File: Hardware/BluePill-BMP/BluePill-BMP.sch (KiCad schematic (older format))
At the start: 18 parts, among them J1 SWO, J2 JTAG, J3 GDB_COMM, J4 VCC, J5 GND, J6 LogicAna, U1 FT232RL_Breakout, U2 STM32F103 BluePill

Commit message: - JTAG over SPI
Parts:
- removed J1: SWO, Connector_PinHeader_2.54mm:PinHeader_1x02_P2.54mm_Vertical, symbol Connector_Generic:Conn_01x02
- added J1: Conn_01x08, Connector_PinHeader_2.54mm:PinHeader_1x08_P2.54mm_Vertical, symbol Connector_Generic:Conn_01x08
- added J7: Conn_01x11, Connector_PinHeader_2.54mm:PinHeader_1x11_P2.54mm_Vertical, symbol Connector_Generic:Conn_01x11
- added J8, J9: Conn_01x05, Connector_PinHeader_2.54mm:PinHeader_1x05_P2.54mm_Vertical, symbol Connector_Generic:Conn_01x05
- J3: footprint Connector_PinHeader_2.54mm:PinHeader_1x04_P2.54mm_Horizontal -> Connector_Molex:Molex_KK-254_AE-6410-04A_1x04_P2.54mm_Vertical
- J4: footprint Connector_PinHeader_2.54mm:PinHeader_1x03_P2.54mm_Vertical -> Connector_PinHeader_2.54mm:PinHeader_1x02_P2.54mm_Vertical; symbol Connector_Generic:Conn_01x03 -> Connector_Generic:Conn_01x02
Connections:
- net +3V3: no longer J4.3 (Pin_3)
- net BRST: now also U2.27 (PA2), J7.11 (Pin_11); no longer U2.5 (PA8)
- net BTCK: now also U2.26 (PA1), J7.8 (Pin_8)
- net BTDI: now also J7.6 (Pin_6)
- net BTDO: now also J7.7 (Pin_7)
- net BTEST: now also U2.29 (PA4), J7.9 (Pin_9); no longer U2.26 (PA1)
- net BTMS: now also U2.28 (PA3), J7.10 (Pin_10); no longer U2.29 (PA4)
- net GDB_RX: now also U2.7 (PA10); no longer U2.28 (PA3)
- net GDB_TX: now also U2.6 (PA9); no longer U2.27 (PA2)
- net LEDG: now also J7.5 (Pin_5)
- net TRACESWO: now also J1.2 (Pin_2)
- net VREF: now also J9.1 (Pin_1)
- net PB12: now reaches U2.1 (PB12)
- net PB12: now also J8.1 (Pin_1)
- net PA15: now reaches U2.10 (PA15)
- net PA15: now also J1.1 (Pin_1)
- net PB4: now reaches U2.12 (PB4)
- net PB4: now also J1.3 (Pin_3)
- net PB5: now reaches U2.13 (PB5)
- net PB5: now also J1.4 (Pin_4)
- net PB6: now reaches U2.14 (PB6)
- net PB6: now also J1.5 (Pin_5)
- net PB7: now reaches U2.15 (PB7)
- net PB7: now also J1.6 (Pin_6)
- net PB8: now reaches U2.16 (PB8)
- net PB8: now also J1.7 (Pin_7)
- net PB9: now reaches U2.17 (PB9)
- net PB9: now also J1.8 (Pin_8)
- net PB13: now reaches U2.2 (PB13)
- net PB13: now also J8.2 (Pin_2)
- net VBAT: now reaches U2.21 (VBat)
- net VBAT: now also J9.5 (Pin_5)
- net PC13: now reaches U2.22 (PC13)
- net PC13: now also J9.4 (Pin_4)
- net PC14: now reaches U2.23 (PC14)
- net PC14: now also J9.3 (Pin_3)
- net PC15: now reaches U2.24 (PC15)
- net PC15: now also J9.2 (Pin_2)
- net PB14: now reaches U2.3 (PB14)
- net PB14: now also J8.3 (Pin_3)
- net PB1: now reaches U2.34 (PB1)
- net PB1: now also J7.4 (Pin_4)
- net PB10: now reaches U2.35 (PB10)
- net PB10: now also J7.3 (Pin_3)
- net PB11: now reaches U2.36 (PB11)
- net PB11: now also J7.2 (Pin_2)
- net RST: now reaches U2.37 (RST)
- net RST: now also J7.1 (Pin_1)
- net PB15: now reaches U2.4 (PB15)
- net PB15: now also J8.4 (Pin_4)
- new net PA8: J8.5 (Pin_5), U2.5 (PA8)
- no-connect marks 47 -> 26
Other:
- note added: "USART1: GDB Port\nTRACESWO: External device or Optional FT232 Breakout\nSPI: JTAG interface (also supports bit-bang)\nTIM2: JTMS signal generation\nGPI: LEDG, JTAG (partial)"
- moved on the sheet: D1, J3, J5, R7, R8, R9, U1

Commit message: Updated Hardware Schematics and Boards
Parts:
- removed J9: Conn_01x05, Connector_PinHeader_2.54mm:PinHeader_1x05_P2.54mm_Vertical, symbol Connector_Generic:Conn_01x05
- removed R1: 330, Resistor_THT:R_Axial_DIN0204_L3.6mm_D1.6mm_P7.62mm_Horizontal, symbol Device:R
- added C1: 100nF, Capacitor_THT:C_Disc_D4.3mm_W1.9mm_P5.00mm, symbol Device:C
- added R10, R11, R9: 330, Resistor_THT:R_Axial_DIN0204_L3.6mm_D1.6mm_P7.62mm_Horizontal, symbol Device:R
- J1: value Conn_01x08 -> Conn_01x07; footprint Connector_PinHeader_2.54mm:PinHeader_1x08_P2.54mm_Vertical -> Connector_PinHeader_2.54mm:PinHeader_1x07_P2.54mm_Vertical; symbol Connector_Generic:Conn_01x08 -> Connector_Generic:Conn_01x07
- J3: renamed from J7; footprint Connector_PinHeader_2.54mm:PinHeader_1x11_P2.54mm_Vertical -> Connector_PinHeader_2.54mm:PinHeader_1x13_P2.54mm_Vertical; symbol Connector_Generic:Conn_01x11 -> Connector_Generic:Conn_01x13
- J8: renamed from J6; footprint Connector_PinHeader_2.54mm:PinHeader_1x06_P2.54mm_Vertical -> Connector_PinHeader_2.54mm:PinHeader_1x07_P2.54mm_Vertical; symbol Connector_Generic:Conn_01x06 -> Connector_Generic:Conn_01x07
- renumbered J8 to J2, J3 to J4, J4 to J5, J5 to J6, J2 to J7, R7 to R1, R8 to R2, R9 to R3, R2 to R4, R3 to R5, R4 to R6, R5 to R7, R6 to R8
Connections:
- net PA8 is gone; now on net BTEST: J2.5 (Pin_5), U2.5 (PA8)
- net PB12 is gone; now on net BRST: J2.1 (Pin_1), U2.1 (PB12)
- net PB13 is gone; now on net BTCK: J2.2 (Pin_2), U2.2 (PB13)
- net PB14 is gone; now on net JTDO: J2.3 (Pin_3), U2.3 (PB14)
- net PB15 is gone; now on net BTDI: J2.4 (Pin_4), U2.4 (PB15)
- net +3V3: now also C1.1
- net BRST: no longer J3.11 (Pin_11), U2.27 (PA2)
- net BTCK: now also J1.4 (Pin_4), U2.14 (PB6); no longer J3.8 (Pin_8), U2.26 (PA1), U2.30 (PA5)
- net BTDI: now also R11.2; no longer J3.6 (Pin_6), U2.32 (PA7)
- net BTEST: no longer J3.9 (Pin_9), U2.29 (PA4)
- net BTMS: now also J1.5 (Pin_5), U2.15 (PB7); no longer J3.10 (Pin_10), U2.28 (PA3)
- net GND: now also J7.13 (Pin_13), J8.7 (Pin_7), C1.2
- net JTDO: now also R11.1
- net LEDG: now also J3.10 (Pin_10); no longer J3.5 (Pin_5)
- net PB1: now also J3.11 (Pin_11); no longer J3.4 (Pin_4)
- net PB5: now also J1.3 (Pin_3); no longer J1.4 (Pin_4)
- net PB8: now also J1.6 (Pin_6); no longer J1.7 (Pin_7)
- net PB9: now also J1.7 (Pin_7); no longer J1.8 (Pin_8)
- net PC13: now also J3.1 (Pin_1)
- net TRACESWO: now also J1.1 (Pin_1); no longer J1.2 (Pin_2)
- net VREF: now also J3.2 (Pin_2)
- net JTXD: now reaches J7.12 (Pin_12)
- net JTXD: now also R9.2
- net JRXD: now reaches J7.14 (Pin_14)
- net JRXD: now also R10.2
- net BTDO renamed PA5
- net PA5: now also U2.30 (PA5); no longer U2.31 (PA6)
- net PA15: no longer names the net of U2.10 (PA15)
- net PA15: no longer J1.1 (Pin_1)
- net PB10 renamed BTXD
- net BTXD: now also J3.12 (Pin_12), R10.1; no longer J3.3 (Pin_3)
- net PB11 renamed BRXD
- net BRXD: now also J3.13 (Pin_13), R9.1; no longer J3.2 (Pin_2)
- net PB4: no longer names the net of U2.12 (PB4)
- net PB4: no longer J1.3 (Pin_3)
- removed net PB6: J1.5 (Pin_5), U2.14 (PB6)
- removed net PB7: J1.6 (Pin_6), U2.15 (PB7)
- net PC14: no longer names the net of U2.23 (PC14)
- net PC15: no longer names the net of U2.24 (PC15)
- net RST: no longer names the net of U2.37 (RST)
- net RST: no longer J3.1 (Pin_1)
- net VBAT: no longer names the net of U2.21 (VBat)
- new net PA1: J3.3 (Pin_3), U2.26 (PA1)
- new net PA2: J3.4 (Pin_4), U2.27 (PA2)
- new net PA3: J3.5 (Pin_5), U2.28 (PA3)
- new net PA4: J3.6 (Pin_6), U2.29 (PA4)
- new net PA6: J3.8 (Pin_8), U2.31 (PA6)
- new net PA7: J3.9 (Pin_9), U2.32 (PA7)
- no-connect marks 26 -> 30
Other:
- note added: "SN74CB3T1G125\nSWO switch"
- moved on the sheet: J2

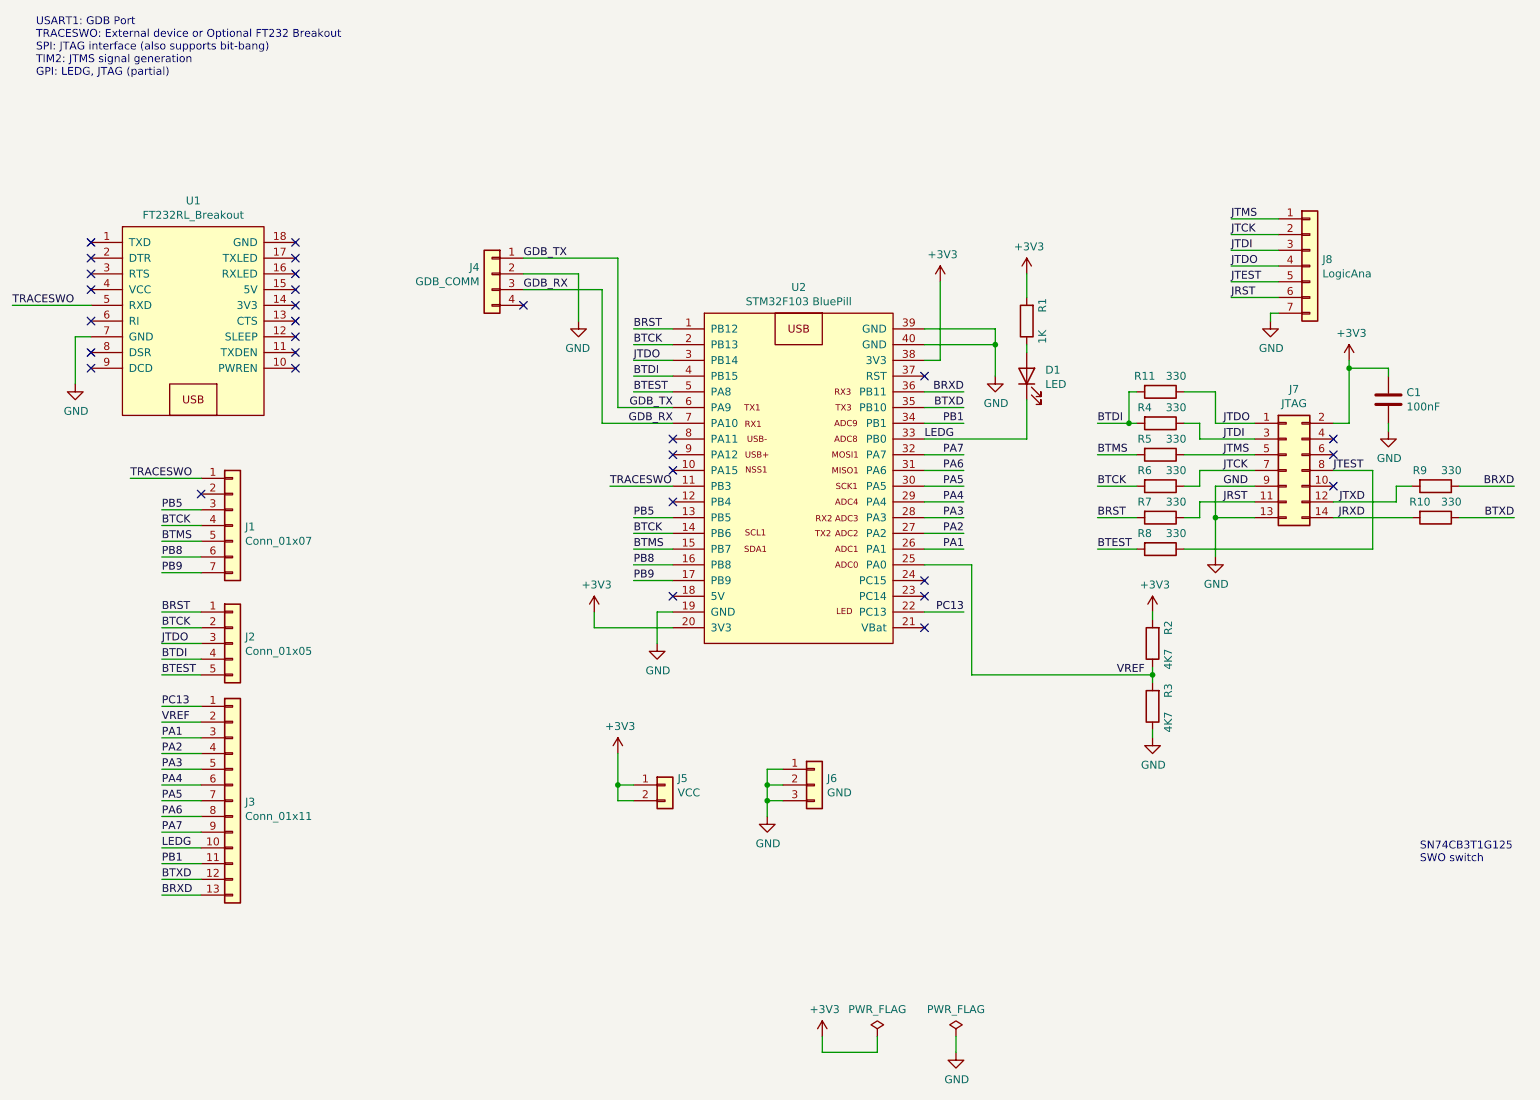
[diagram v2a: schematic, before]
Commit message: Fixed Bluepill schematics
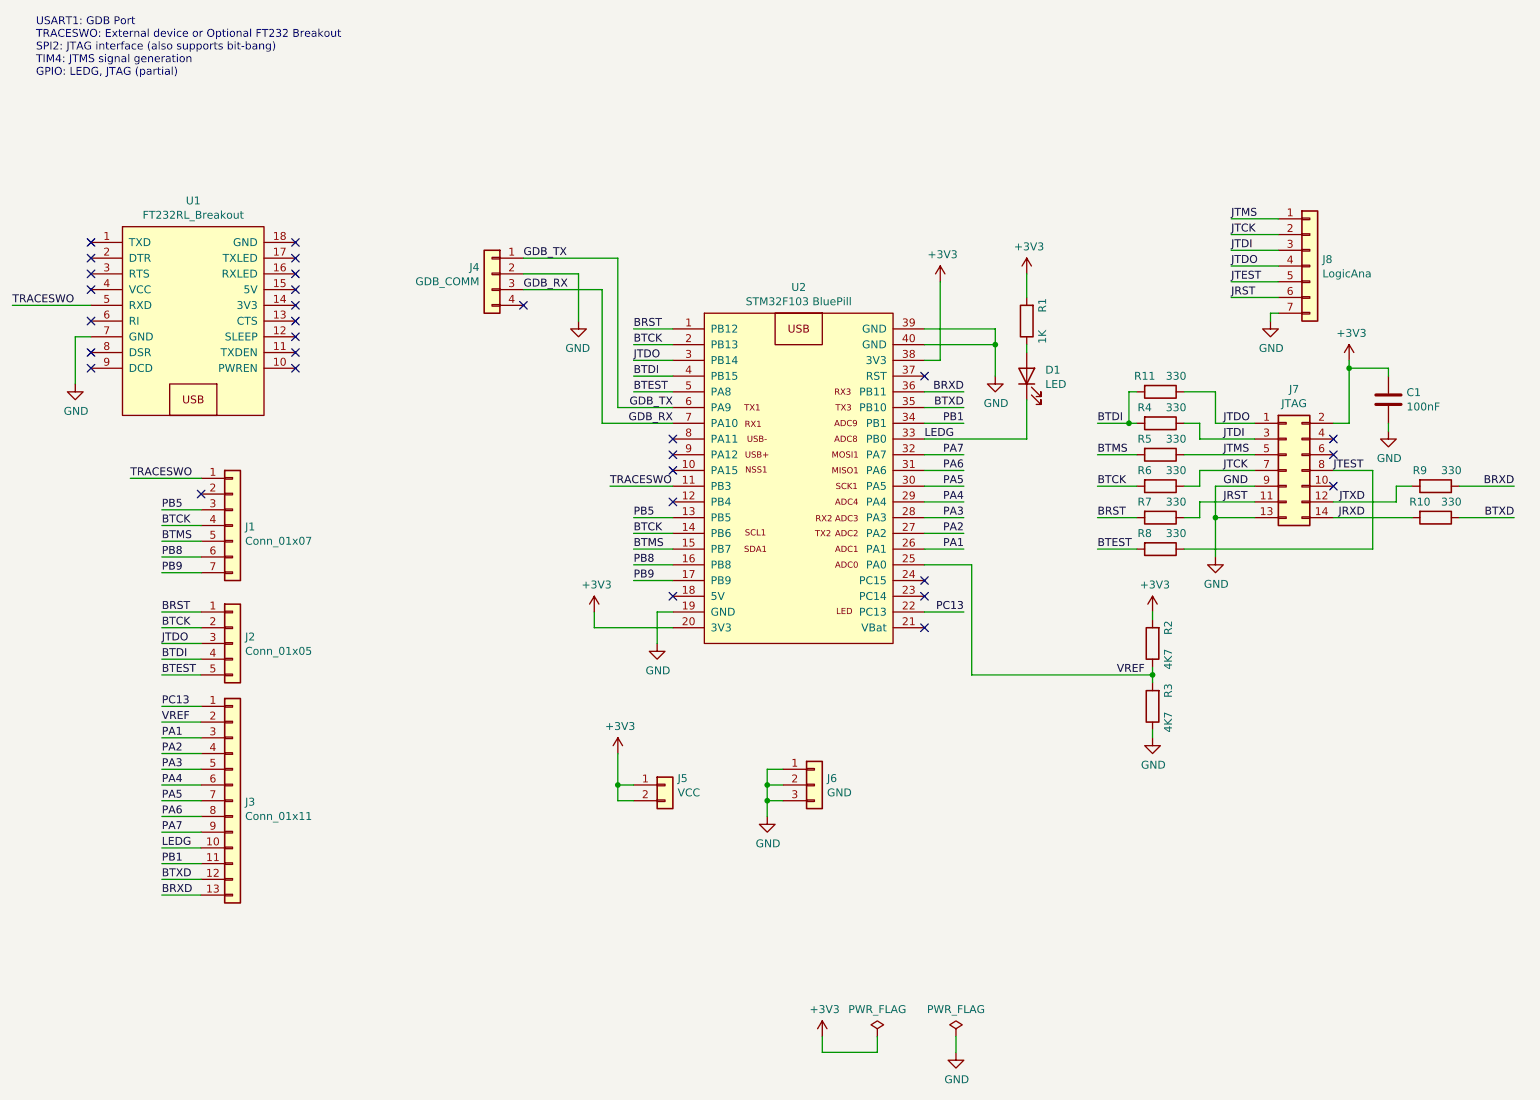
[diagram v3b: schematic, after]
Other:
- note added: "USART1: GDB Port\nTRACESWO: External device or Optional FT232 Breakout\nSPI2: JTAG interface (also supports bit-bang)\nTIM4: JTMS signal generation\nGPIO: LEDG, JTAG (partial)"
- note removed: "SN74CB3T1G125\nSWO switch"
- note removed: "USART1: GDB Port\nTRACESWO: External device or Optional FT232 Breakout\nSPI: JTAG interface (also supports bit-bang)\nTIM2: JTMS signal generation\nGPI: LEDG, JTAG (partial)"
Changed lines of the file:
@@
 	7600 4250 7850 4250
 Text Notes 850  1250 0    50   ~ 0
-USART1: GDB Port\nTRACESWO: External device or Optional FT232 Breakout\nSPI: JTAG interface (also supports bit-bang)\nTIM2: JTMS signal generation\nGPI: LEDG, JTAG (partial)
+USART1: GDB Port\nTRACESWO: External device or Optional FT232 Breakout\nSPI2: JTAG interface (also supports bit-bang)\nTIM4: JTMS signal generation\nGPIO: LEDG, JTAG (partial)
 Text Label 7600 4250 0    50   ~ 0
 BTEST
@@
 Text Label 6750 4650 2    50   ~ 0
 PC13
-Text Notes 9650 6250 0    50   ~ 0
-SN74CB3T1G125\nSWO switch
 Wire Wire Line
 	7850 3850 7600 3850

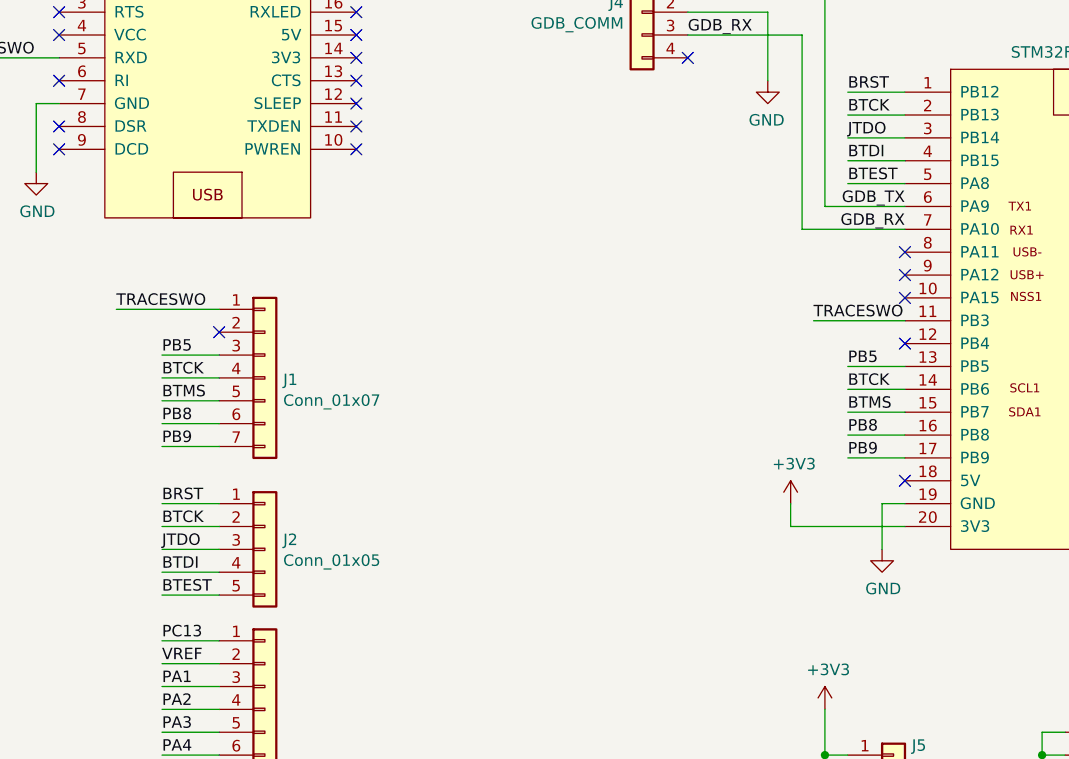
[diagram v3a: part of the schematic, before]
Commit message: Revised BluePill Prototype board
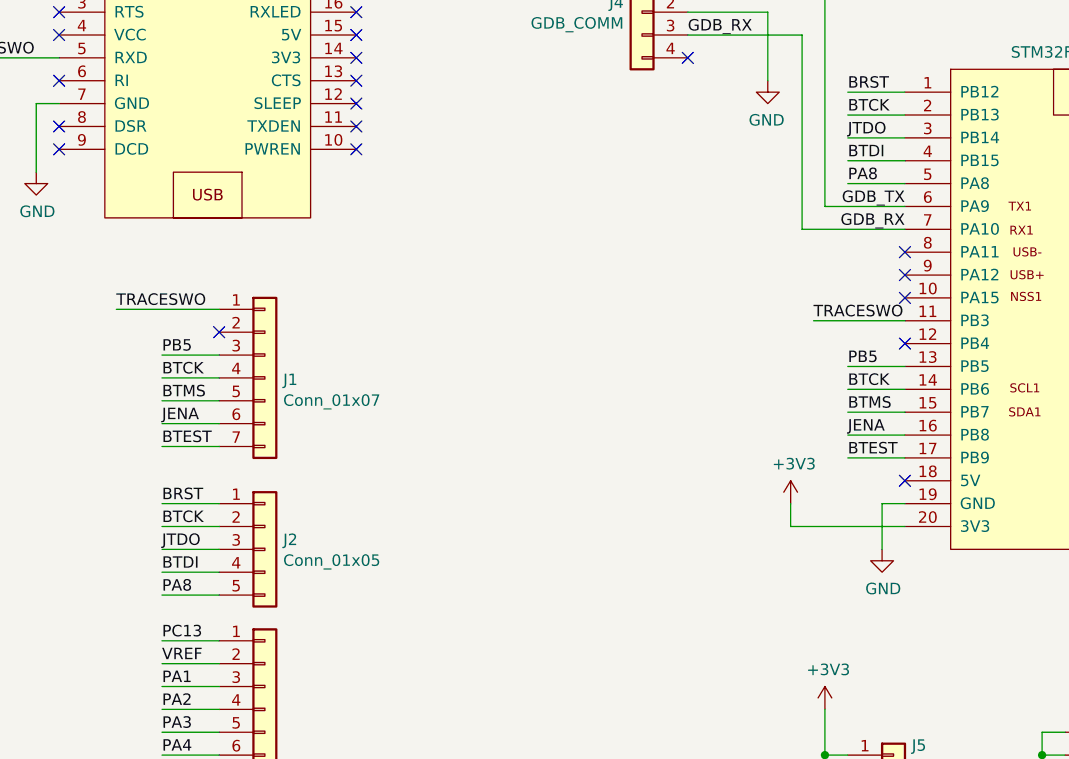
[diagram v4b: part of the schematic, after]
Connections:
- net PB9 is gone; now on net BTEST: J1.7 (Pin_7), U2.17 (PB9)
- net BTEST: no longer J2.5 (Pin_5), U2.5 (PA8)
- net PB8 renamed JENA
- new net PA8: J2.5 (Pin_5), U2.5 (PA8)
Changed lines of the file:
@@
 Sheet 1 1
 Title "MSPBMP Development Protoboard"
-Date "2021-11-07"
-Rev "1"
+Date "2021-12-04"
+Rev "2"
 Comp "Mathias Gruber"
 Comment1 "With optional TRACE SWO using FT232RL"
@@
 	9350 4250 8150 4250
 Text Label 4650 3250 0    50   ~ 0
-BTEST
+PA8
 Text Label 9100 3750 0    50   ~ 0
 JTEST
@@
 PA7
 Text Label 4650 4350 0    50   ~ 0
-PB8
-Text Label 4650 4450 0    50   ~ 0
-PB9
+JENA
 Text Label 1450 3800 0    50   ~ 0
 TRACESWO
 Text Label 1650 4000 0    50   ~ 0
 PB5
+Text Label 1650 5050 0    50   ~ 0
+PA8
 Text Label 1650 4300 0    50   ~ 0
-PB8
-Text Label 1650 4400 0    50   ~ 0
-PB9
+JENA
 Wire Wire Line
 	4550 5550 4550 5750
@@
 Text Label 1650 4750 0    50   ~ 0
 BTCK
-Text Label 1650 5050 0    50   ~ 0
+Text Label 1650 4400 0    50   ~ 0
 BTEST
 Text Label 1650 4200 0    50   ~ 0
@@
 Wire Wire Line
 	8700 2750 8750 2750
+Text Label 4650 4450 0    50   ~ 0
+BTEST
 $EndSCHEMATC
